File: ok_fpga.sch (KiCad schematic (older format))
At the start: 4 parts, among them P2 M-2X10-87759_M

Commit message: cleanup from Eagle import
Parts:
- R153, R154: footprint adc_dac_v1:R0603 -> Resistor_SMD:R_0603_1608Metric; symbol adc_dac_v1-eagle-import:R-US_R0603 -> Device:R_US
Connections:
- net labels added: +3V3
- net labels removed: 3V3
- wire segments 183 -> 187

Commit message: completed gp adc
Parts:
- removed P2: M-2X10-87759_M, adc_dac_v1:87759-20_M, symbol adc_dac_v1-eagle-import:M-2X10-87759_M
- added J?: Conn_02x10_Odd_Even, symbol Connector_Generic:Conn_02x10_Odd_Even
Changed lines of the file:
@@
 $Descr User 12505 8743
 encoding utf-8
-Sheet 8 10
+Sheet 6 10
 Title ""
 Date ""
@@
 $EndComp
 $Comp
-L adc_dac_v1-eagle-import:M-2X10-87759_M P2
-U 1 1 166FC715
-P 4800 6300
-F 0 "P2" H 4650 6830 59  0000 L BNN
-F 1 "M-2X10-87759_M" H 4650 5600 59  0000 L BNN
-F 2 "adc_dac_v1:87759-20_M" H 4800 6300 50  0001 C CNN
-F 3 "" H 4800 6300 50  0001 C CNN
-	1    4800 6300
-	1    0    0    -1
-$EndComp
-$Comp
 L Device:R_US R153
 U 1 1 19684600
@@
 	1    0    0    -1
 $EndComp
-Text GLabel 3900 5900 2    70   BiDi ~ 0
+Text GLabel 4000 5900 2    70   BiDi ~ 0
 D0_CSB
 Text GLabel 3000 2900 2    50   BiDi ~ 0
 D0_CSB
-Text GLabel 3900 6000 2    70   BiDi ~ 0
+Text GLabel 4000 6000 2    70   BiDi ~ 0
 D0_SDI
 Text GLabel 3000 3000 2    50   BiDi ~ 0
 D0_SDI
-Text GLabel 3900 6100 2    70   BiDi ~ 0
+Text GLabel 4000 6100 2    70   BiDi ~ 0
 D0_SCLK
 Text GLabel 3000 3100 2    50   BiDi ~ 0
 D0_SCLK
-Text Label 3900 6200 0    70   ~ 0
+Text Label 4000 6200 0    70   ~ 0
 GP_0
 Text Label 5500 3800 0    50   ~ 0
 GP_0
-Text Label 3900 6300 0    70   ~ 0
+Text Label 4000 6300 0    70   ~ 0
 GP_1
 Text Label 3000 3900 0    50   ~ 0
 GP_1
-Text Label 3900 6400 0    70   ~ 0
+Text Label 4000 6400 0    70   ~ 0
 GP_2
 Text Label 5500 3900 0    50   ~ 0
 GP_2
-Text Label 3900 6500 0    70   ~ 0
+Text Label 4000 6500 0    70   ~ 0
 GP_3
 Text Label 3000 4000 0    50   ~ 0
 GP_3
-Text Label 3900 6600 0    70   ~ 0
+Text Label 4000 6600 0    70   ~ 0
 GP_4
 Text Label 5500 4000 0    50   ~ 0
 GP_4
-Text Label 3900 6700 0    70   ~ 0
+Text Label 4000 6700 0    70   ~ 0
 GP_5
 Text Label 3000 4100 0    50   ~ 0
@@
 A3_EN0_HV
 Wire Wire Line
-	3900 5900 4500 5900
+	4000 5900 4600 5900
 Wire Wire Line
 	2900 2900 3000 2900
 Wire Wire Line
-	3900 6000 4500 6000
+	4000 6000 4600 6000
 Wire Wire Line
 	2900 3000 3000 3000
 Wire Wire Line
-	4500 6100 3900 6100
+	4600 6100 4000 6100
 Wire Wire Line
 	2900 3100 3000 3100
 Wire Wire Line
-	4500 6200 3900 6200
+	4600 6200 4000 6200
 Wire Wire Line
 	5400 3800 5500 3800
 Wire Wire Line
-	4500 6300 3900 6300
+	4600 6300 4000 6300
 Wire Wire Line
 	2900 3900 3000 3900
 Wire Wire Line
-	4500 6400 3900 6400
+	4600 6400 4000 6400
 Wire Wire Line
 	5400 3900 5500 3900
 Wire Wire Line
-	4500 6500 3900 6500
+	4600 6500 4000 6500
 Wire Wire Line
 	2900 4000 3000 4000
 Wire Wire Line
-	4500 6600 3900 6600
+	4600 6600 4000 6600
 Wire Wire Line
 	5400 4000 5500 4000
 Wire Wire Line
-	4500 6700 3900 6700
+	4600 6700 4000 6700
 Wire Wire Line
 	2900 4100 3000 4100
 Wire Wire Line
-	4500 6800 3900 6800
+	4600 6800 4000 6800
 Wire Wire Line
 	5100 6800 5400 6800
@@
 L power:GND #PWR0144
 U 1 1 60BB36D1
-P 3900 6800
-F 0 "#PWR0144" H 3900 6550 50  0001 C CNN
-F 1 "GND" H 3905 6627 50  0001 C CNN
-F 2 "" H 3900 6800 50  0001 C CNN
-F 3 "" H 3900 6800 50  0001 C CNN
-	1    3900 6800
+P 4000 6800
+F 0 "#PWR0144" H 4000 6550 50  0001 C CNN
+F 1 "GND" H 4005 6627 50  0001 C CNN
+F 2 "" H 4000 6800 50  0001 C CNN
+F 3 "" H 4000 6800 50  0001 C CNN
+	1    4000 6800
 	1    0    0    -1
 $EndComp
@@
 Wire Wire Line
 	6500 6000 6600 6000
+$Comp
+L Connector_Generic:Conn_02x10_Odd_Even J?
+U 1 1 629450E5
+P 4800 6300
+F 0 "J?" H 4850 6917 50  0000 C CNN
+F 1 "Conn_02x10_Odd_Even" H 4850 6826 50  0000 C CNN
+F 2 "" H 4800 6300 50  0001 C CNN
+F 3 "~" H 4800 6300 50  0001 C CNN
+	1    4800 6300
+	1    0    0    -1
+$EndComp
 $EndSCHEMATC

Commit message: add 2.5 V supply
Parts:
- OK1: footprint adc_dac_v1:OPALKELLY_XEM6010 -> covg-kicad:OPALKELLY_XEM6010; symbol adc_dac_v1-eagle-import:OPALKELLY_XEM6310 -> covg-kicad:OPALKELLY_XEM7310
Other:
- note added: "Bank 13: 3.3V always\nMC1 64 and 66-76 MC2 64 and 66-76 \n(24 total)"
- note added: "Bank 34: default 3.3V, \nchange by ferrite bead (FB8)\non MC1 \n(total of 48)"
- note added: "Bank 35: default 3.3V, \nchange by ferrite bead (FB9)\nMC2 2\n(total of 50)"
- note added: "IO voltage for bank 34"
- note added: "IO voltage for bank 35"
- note added: "VREF: needed for single-ended IO standards that use a diff. input buffer.\nWe do not need VREF. The FPGA also has an internal VREF which can be used if running at or below 400 MHz. \nMost relevant to memory interfaces."
- moved on the sheet: J?, R153, R154

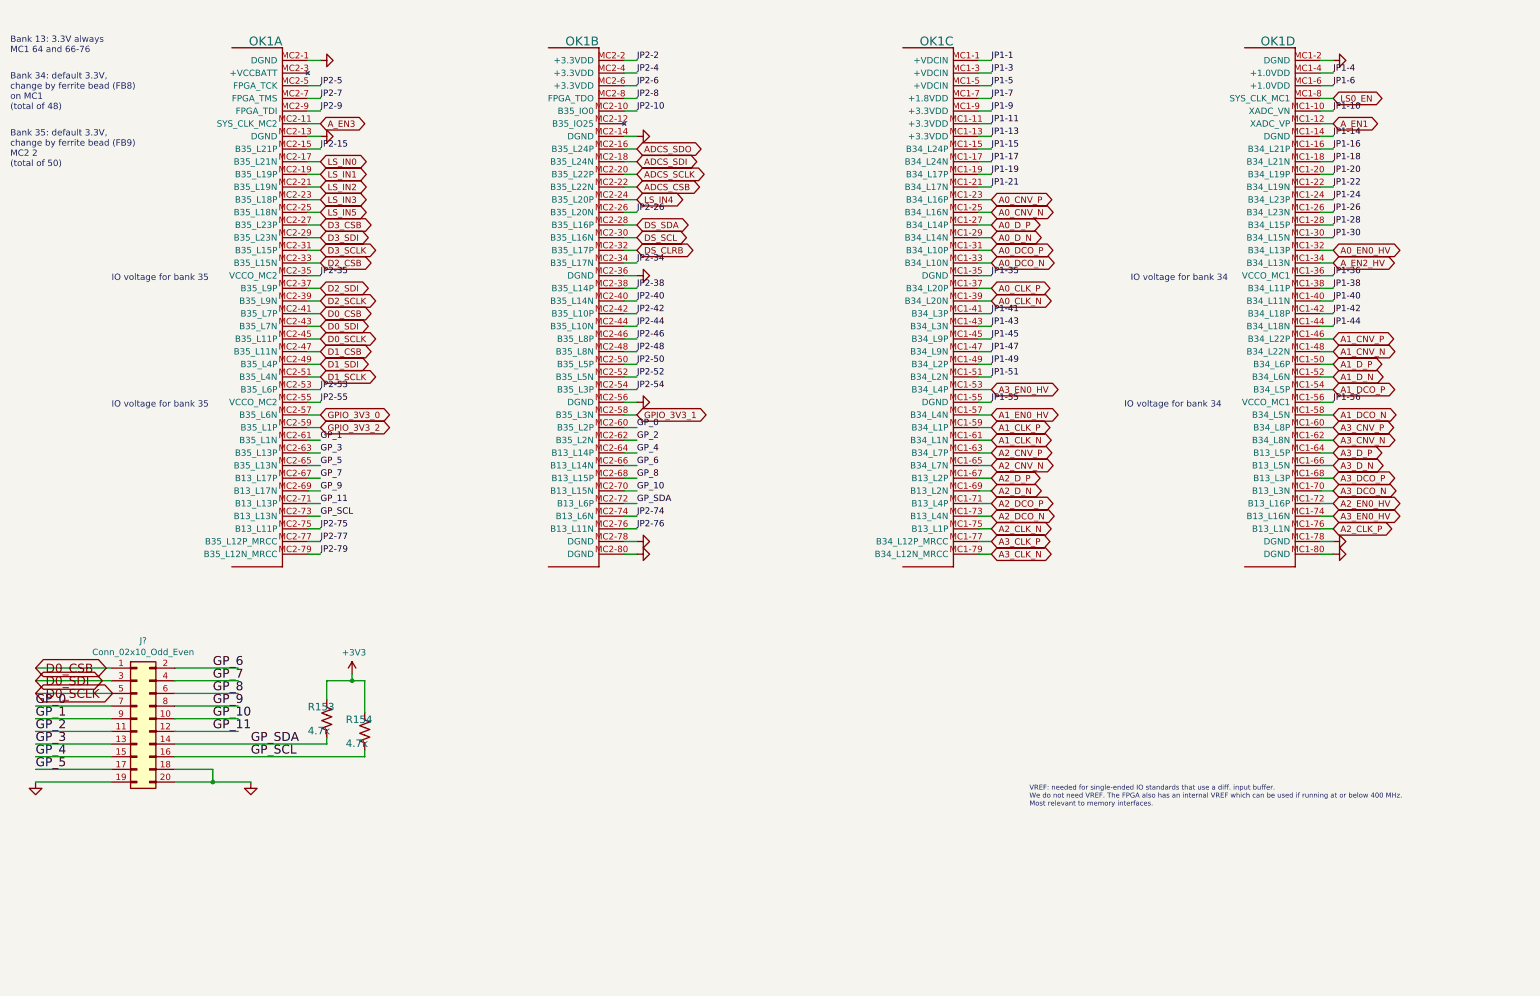
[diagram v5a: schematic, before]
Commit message: modify LVDS connections for AD7960
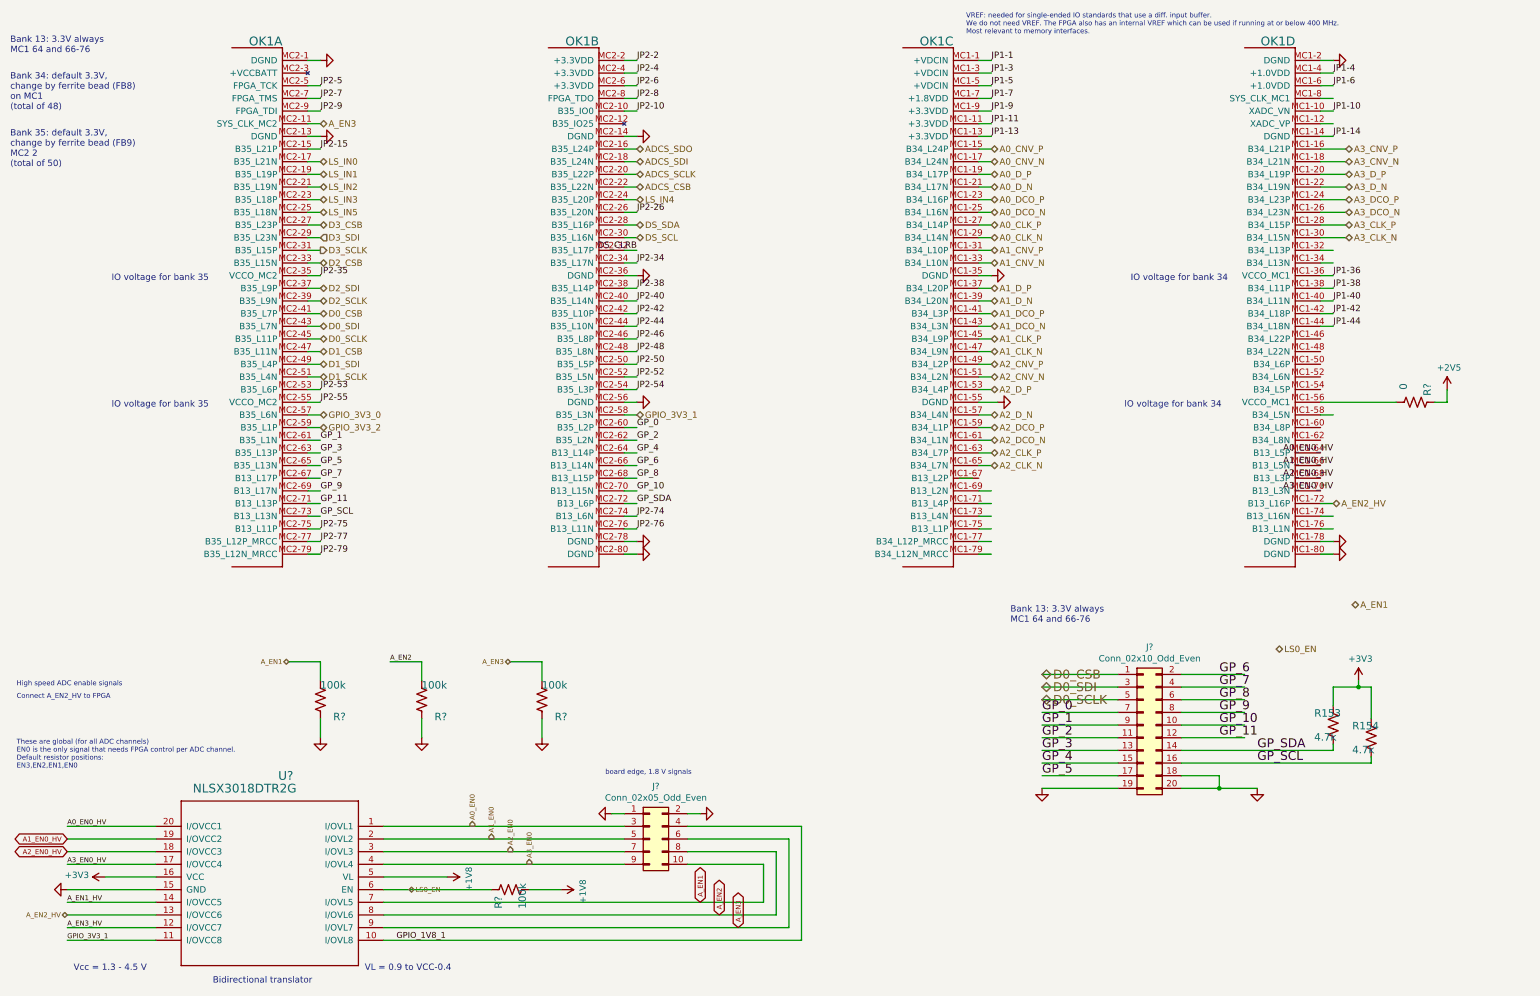
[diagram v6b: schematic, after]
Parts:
- added J?: Conn_02x05_Odd_Even, symbol Connector_Generic:Conn_02x05_Odd_Even
- added R?: 0, Resistor_SMD:R_0603_1608Metric, symbol Device:R_US
- added R? (x4): 100k, Resistor_SMD:R_0603_1608Metric, symbol Device:R_US
- added U?: NLSX3018DTR2G, adc_dac_v1:TSSOP20_4P50X6P60_ONS, symbol adc_dac_v1-eagle-import:NLSX3018DTR2G
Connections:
- net labels added: +1V8, +2V5, A0_EN0, A1_EN0, A2_EN0, A3_EN0, A_EN1_HV, A_EN2, A_EN3_HV, GPIO_1V8_1
- net labels removed: JP1-15, JP1-16, JP1-17, JP1-18, JP1-19, JP1-20, JP1-21, JP1-22, JP1-24, JP1-26, JP1-28, JP1-30, JP1-35, JP1-41, JP1-43, JP1-45, JP1-47, JP1-49, JP1-51, JP1-55, JP1-56
- wire segments 187 -> 218
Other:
- note added: "Bidirectional translator"
- note added: "Connect A_EN2_HV to FPGA"
- note added: "High speed ADC enable signals"
- note added: "These are global (for all ADC channels)\nEN0 is the only signal that needs FPGA control per ADC channel.\nDefault resistor positions: \nEN3,EN2,EN1,EN0 \n0,0,0,FPGA (A_EN2_HV is high-Z)\n\ndriving EN2 high outputs test\npatterns on the LVDS interface"
- note added: "VL = 0.9 to VCC-0.4"
- note added: "Vcc = 1.3 - 4.5 V"
- note added: "board edge, 1.8 V signals"
- moved on the sheet: J?, R153, R154

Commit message: moved level shifters to FPGA
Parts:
- added J?: QWIIC_CONNECTORJS-1MM, 1X04_1MM_RA, symbol SparkFun-Connectors:QWIIC_CONNECTORJS-1MM
- added R?: 0, Resistor_SMD:R_0603_1608Metric, symbol Device:R_US
- added R? (x2): 3.3k, Resistor_SMD:R_0603_1608Metric, symbol Device:R_US
- added R? (x12): 3.3k, Resistor_SMD:R_0603_1608Metric, symbol Device:R_Small_US
- added R?: 100k, Resistor_SMD:R_0603_1608Metric, symbol Device:R_Small_US
- added U?: PCA9306, symbol Interface:PCA9306
- R? (x3): symbol Device:R_US -> Device:R_Small_US
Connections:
- net labels added: DC_SCL[0], DC_SCL[1], DC_SCL[2], DC_SCL[3], DC_SDA[0], DC_SDA[1], DC_SDA[2], DC_SDA[3], GPIO_1V8_0, ISEL[0..3], ISEL[0], ISEL[1], ISEL[2], ISEL[3]
- net labels removed: GPIO_1V8_1, GPIO_3V3_2, JP1-36, JP1-38, JP1-40, JP1-42, JP1-44, JP2-74, JP2-75, JP2-76, LS_IN0, LS_IN1, LS_IN2, LS_IN3, LS_IN5
- wire segments 218 -> 249
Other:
- note added: "Level shifter is not for I2C"
- note added: "Ok for 2.5 V \nto TMUX since \nref to Gnd"
- note added: "SparkFun qwiic connector\nSM04B-SRSS-TB\n3.3 V VCC"
- note added: "These are global (for all ADC channels)\nEN0 is the only signal that needs FPGA control per ADC channel.\nDefault settings: \nEN3,EN2,EN1,EN0 \n0,0,0,FPGA (A_EN2_HV is high-Z)\n\ndriving EN2 high outputs test\npatterns on the LVDS interface"
- note added: "What is VCCBATT?\nAdd in 2 more high-speed digital SPI"
- note removed: "Connect A_EN2_HV to FPGA"
- note removed: "High speed ADC enable signals"
- note removed: "These are global (for all ADC channels)\nEN0 is the only signal that needs FPGA control per ADC channel.\nDefault resistor positions: \nEN3,EN2,EN1,EN0 \n0,0,0,FPGA (A_EN2_HV is high-Z)\n\ndriving EN2 high outputs test\npatterns on the LVDS interface"
- moved on the sheet: J?, OK1A, OK1B, OK1C, OK1D, R153, R154, R?, U?

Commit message: updates to high-speed DAC
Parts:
- added J?: Conn_Coaxial, symbol Connector:Conn_Coaxial
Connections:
- net labels added: ADCS_BUSY, ADCS_CONVST, ADCS_SDOA, ADCS_SDOB, D4_CSB, D4_SCLK, D4_SDI, D5_CSB, D5_SCLK, D5_SDI, DS_CSB, DS_SCLK, DS_SDI, DS_SDO, GPIO_2V5_0, QW_SCL, QW_SDA
- net labels removed: ADCS_SDO, DS_CLRB, DS_SCL, DS_SDA, GPIO_3V3_1, JP1-1, JP1-10, JP1-11, JP1-13, JP1-14, JP1-3, JP1-5, JP1-7, JP1-9, JP2-10, JP2-15, JP2-2, JP2-26, JP2-34, JP2-35, JP2-38, JP2-4, JP2-40, JP2-42, JP2-44, JP2-46, JP2-48, JP2-5, JP2-50, JP2-52, JP2-53, JP2-54, JP2-55, JP2-6, JP2-7, JP2-77, JP2-79, JP2-8, JP2-9, LS_IN4
- wire segments 249 -> 239
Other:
- note added: "11 @ 3.3V"
- note added: "2 @ 2.5V"
- note added: "3 @ 3.3 V"
- note added: "3.3 V (leave open)"
- note added: "7 @ 3.3V"
- note added: "ADS8686\n16-chan ADC"
- note added: "DAC80508\n8-chan"
- note added: "Do a check of skew matching between DCO and D \nfor high-speed ADC"
- note added: "SYS_CLK not special other than name"
- moved on the sheet: R?
